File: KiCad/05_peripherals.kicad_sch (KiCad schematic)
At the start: 43 parts, among them IC501 VEML7700-TT, IC502 DS3231MZ+TRL, U501 BME280, U502 DS18B20, U503 LM35-LP, U504 DHT11

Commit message: Firmware refactoring. Beginning
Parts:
- removed D501, D502, D503, D504, D505, D506, D507, D508: WS2812B, LED_SMD:LED_WS2812B_PLCC4_5.0x5.0mm_P3.2mm, symbol LED:WS2812B
- removed R512: 0R, Resistor_SMD:R_0805_2012Metric, symbol Device:R
- added C1, C2, C409: 100nF, Capacitor_SMD:C_0603_1608Metric, symbol Device:C
- added R1, R2, R409: 10kR, Resistor_SMD:R_0805_2012Metric, symbol Device:R
- added SW1, SW2, SW403: ~, esp32_s3_weather_webserver:SW_PUSH_6mm_H5mm, symbol esp32_s3_weather_webserver:SW_PUSH_6mm_H5mm
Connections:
- net +3V3_PER: now also C513.1, C514.1, R509.1, U504.1 (VDD)
- net +5V: no longer C513.1, C514.1, R509.1, U504.1 (VDD)
- net GND: now also C1.1, C1.2, C2.1, C2.2, C409.1, C409.2, SW1.2, SW1.3, SW2.2, SW2.3, SW403.2, SW403.3
- new net: R409.2, SW403.1, SW403.4
- new net: R1.2, SW1.1, SW1.4
- new net: R2.2, SW2.1, SW2.4
- new net +3V3: R1.1, R2.1, R409.1
- no-connect marks 6 -> 5
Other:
- note added: "User BUTTON"
- note added: "User BUTTON Left"
- note added: "User BUTTON Right"
- note removed: "RGB strip"

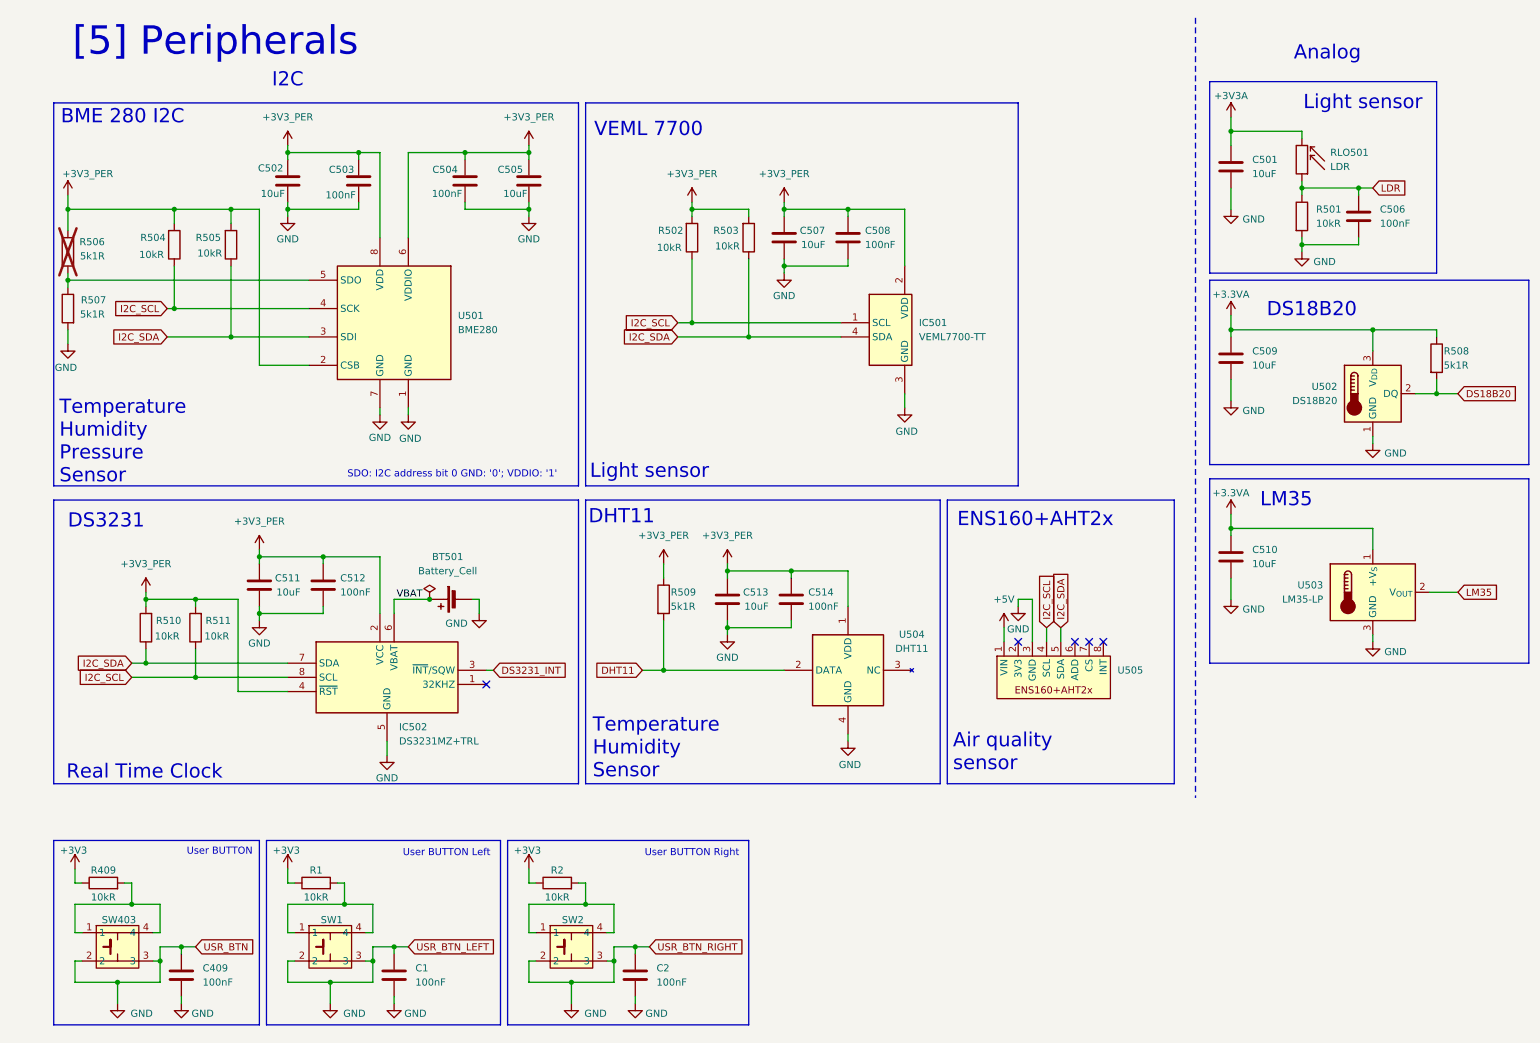
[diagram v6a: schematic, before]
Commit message: Update BME280 Scheme, Add more sensors to firmware
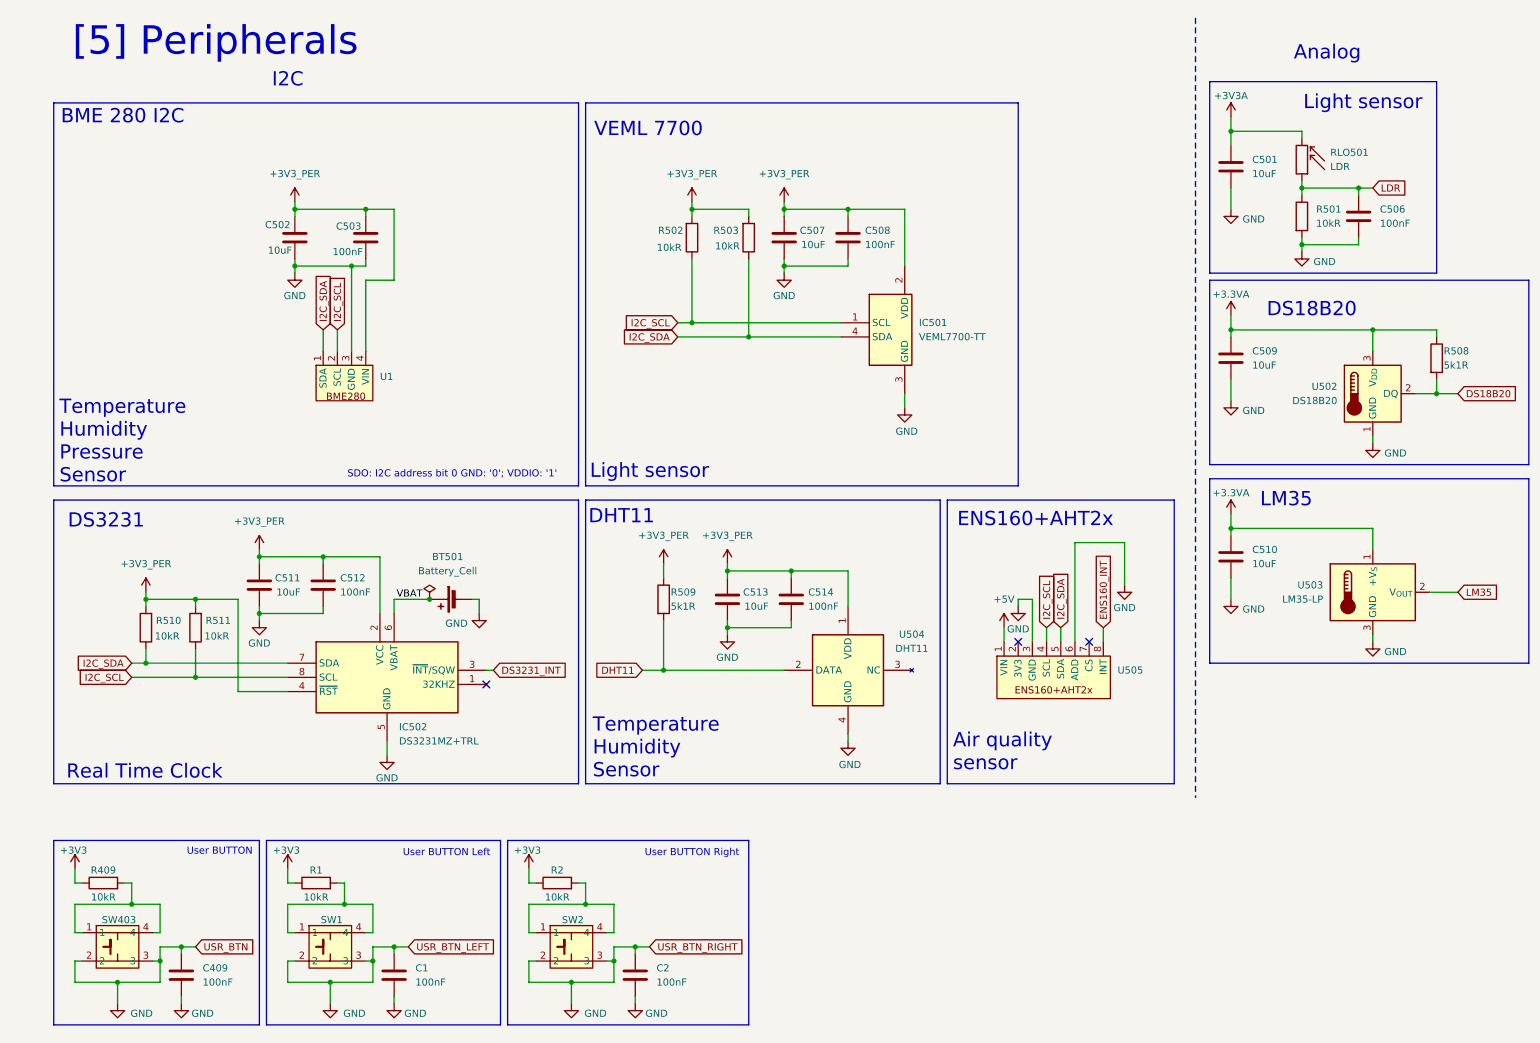
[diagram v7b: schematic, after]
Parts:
- removed C504: 100nF, Capacitor_SMD:C_0603_1608Metric, symbol Device:C
- removed C505: 10uF, Capacitor_SMD:C_0603_1608Metric, symbol Device:C
- removed R504, R505: 10kR, Resistor_SMD:R_0805_2012Metric, symbol Device:R
- removed R506, R507: 5k1R, Resistor_SMD:R_0805_2012Metric, symbol Device:R
- removed U501: BME280, Package_LGA:Bosch_LGA-8_2.5x2.5mm_P0.65mm_ClockwisePinNumbering, symbol Sensor:BME280
- added U1: ~, symbol esp32_s3_weather_webserver:BME280
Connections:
- net +3V3_PER: now also U1.4 (VIN)
- net GND: now also U505.6 (ADD), U1.3 (GND)
- net I2C_SCL: now also U1.2 (SCL)
- net I2C_SDA: now also U1.1 (SDA)
- net ENS160_INT: now reaches U505.8 (INT)
- no-connect marks 5 -> 3
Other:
- moved on the sheet: C502, C503

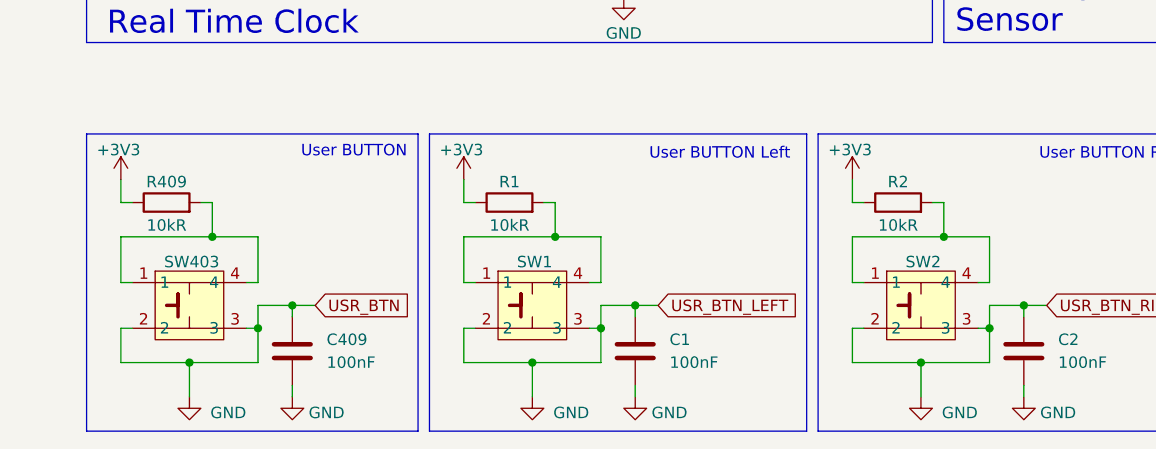
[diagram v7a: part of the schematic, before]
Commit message: Add multisensor wrapper
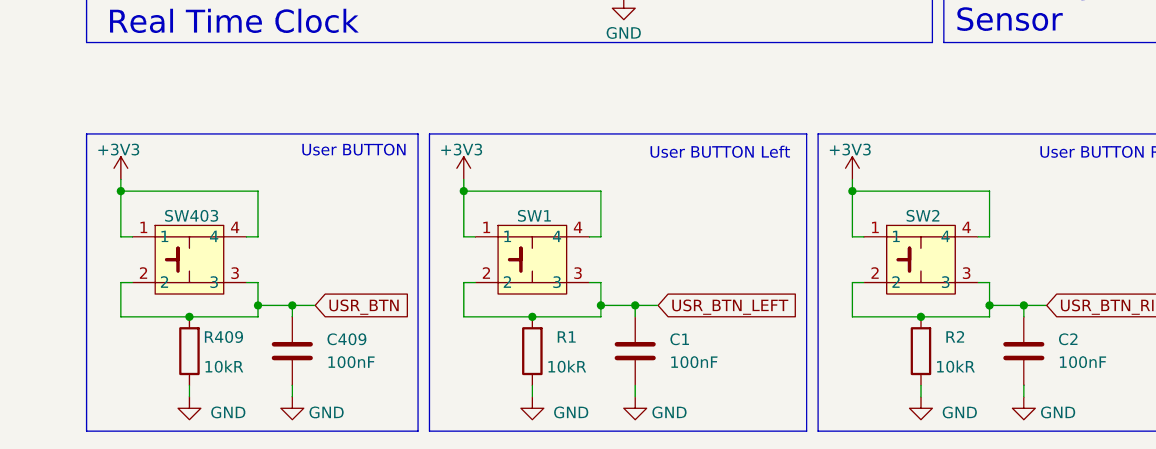
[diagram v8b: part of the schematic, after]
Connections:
- net +3V3: now also SW1.1, SW1.4, SW2.1, SW2.4, SW403.1, SW403.4; no longer R1.1, R2.1, R409.1
- net GND: now also R1.1, R2.1, R409.1; no longer C1.1, C2.1, C409.1, SW1.2, SW1.3, SW2.2, SW2.3, SW403.2, SW403.3
- new net USR_BTN: C409.1, R409.2, SW403.2, SW403.3
- new net USR_BTN_LEFT: C1.1, R1.2, SW1.2, SW1.3
- new net USR_BTN_RIGHT: C2.1, R2.2, SW2.2, SW2.3
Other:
- moved on the sheet: R409, SW403
